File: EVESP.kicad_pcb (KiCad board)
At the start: 2 copper layers, 106 parts, among them J1 Screw_Terminal_01x08, J2 Screw_Terminal_01x06, J3 Conn_01x04, J4 Conn_01x16_Male, J5 Conn_01x16_Female, J6 Conn_01x20_Female, J7 Conn_01x20_Male, J8 Screw_Terminal_01x03, J9 Screw_Terminal_01x03, Q1 BC847, Q2 BC847, Q3 BC847, U1 LM7332, U2 MOC3063M, U3 MOC3063M, U4 MOC3063M, U5 LM7332

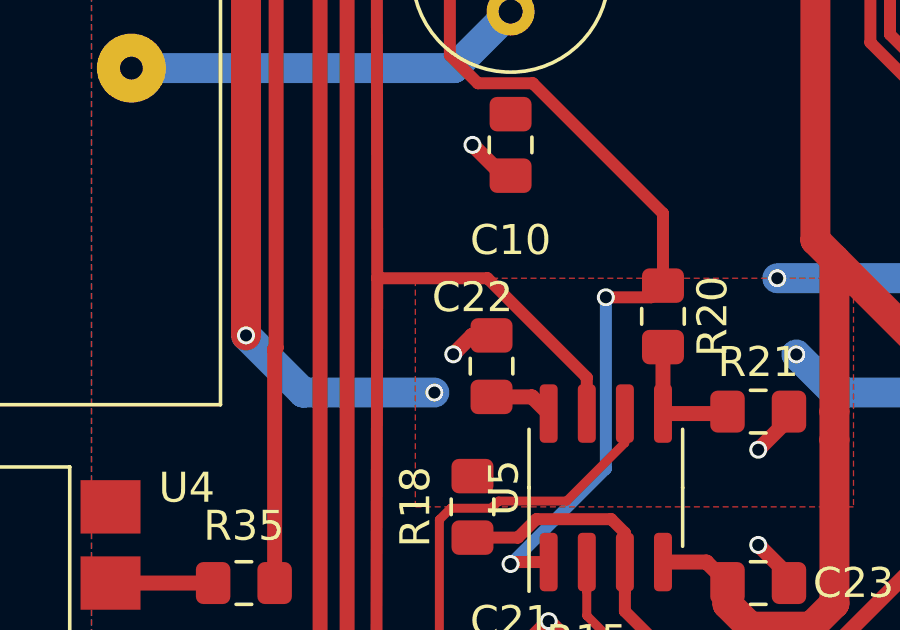
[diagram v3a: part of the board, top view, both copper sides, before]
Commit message: +12V connectivity fixed
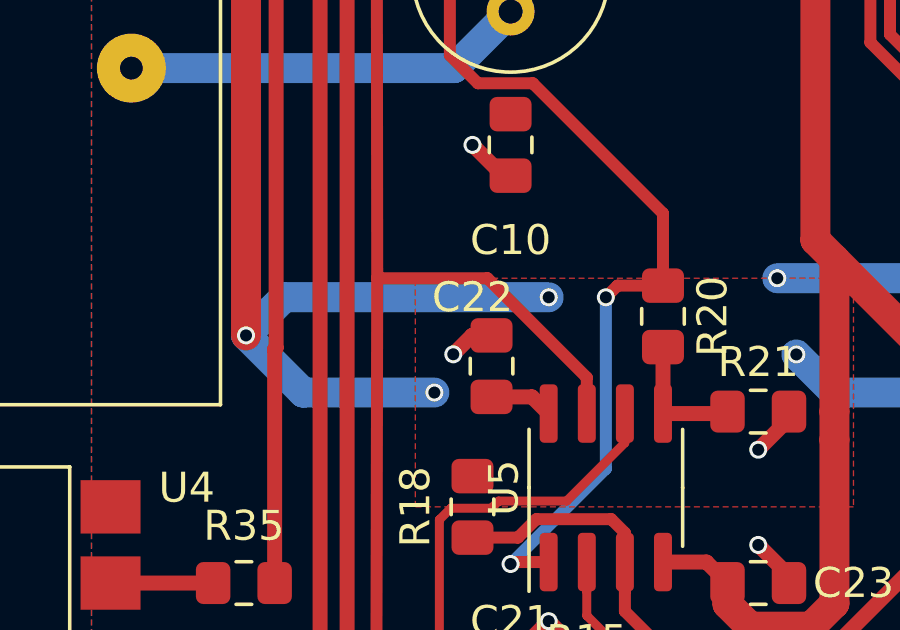
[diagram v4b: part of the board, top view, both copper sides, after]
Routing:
- net +12V: track 112.8 -> 123.4 mm, vias 4 -> 5
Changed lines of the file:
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@@
     (thickness 1.6)
     (drawings 0)
-    (tracks 612)
+    (tracks 615)
     (zones 0)
     (modules 106)
@@
   )
   (setup
-    (last_trace_width 0.5)
+    (last_trace_width 0.4)
     (user_trace_width 0.3)
     (user_trace_width 0.4)
@@
   (segment (start 94.615 133.35) (end 90.24099 133.35) (width 1) (layer B.Cu) (net 4))
   (segment (start 117.475 133.35) (end 118.11 133.35) (width 1) (layer B.Cu) (net 4))
+  (via (at 98.425 130.175) (size 0.6) (drill 0.4) (layers F.Cu B.Cu) (net 4))
+  (segment (start 89.60599 130.175) (end 98.425 130.175) (width 1) (layer B.Cu) (net 4))
+  (segment (start 88.33599 131.445) (end 89.60599 130.175) (width 1) (layer B.Cu) (net 4))
   (segment (start 131.69 142.175) (end 131.055 141.54) (width 0.5) (layer F.Cu) (net 5))
   (segment (start 131.69 142.875) (end 131.69 142.175) (width 0.5) (layer F.Cu) (net 5))
@@
   (segment (start 102.235 129.785) (end 102.235 127.379378) (width 0.4) (layer F.Cu) (net 68))
   (segment (start 98.425 139) (end 97.22 139) (width 0.4) (layer F.Cu) (net 68))
-  (via (at 97.155 139.065) (size 0.6) (drill 0.4) (layers F.Cu B.Cu) (net 68))
-  (segment (start 97.22 139) (end 97.155 139.065) (width 0.4) (layer F.Cu) (net 68))
-  (segment (start 100.33 130.175) (end 101.845 130.175) (width 0.4) (layer F.Cu) (net 68))
-  (segment (start 101.845 130.175) (end 102.235 129.785) (width 0.4) (layer F.Cu) (net 68))
-  (segment (start 100.33 135.89) (end 100.33 130.175) (width 0.4) (layer B.Cu) (net 68))
-  (via (at 100.33 130.175) (size 0.6) (drill 0.4) (layers F.Cu B.Cu) (net 68))
   (segment (start 97.155 139.065) (end 100.33 135.89) (width 0.4) (layer B.Cu) (net 68))
+  (via (at 100.33 130.175) (size 0.6) (drill 0.4) (layers F.Cu B.Cu) (net 68))
+  (segment (start 100.33 135.89) (end 100.33 130.175) (width 0.4) (layer B.Cu) (net 68))
+  (segment (start 97.22 139) (end 97.155 139.065) (width 0.4) (layer F.Cu) (net 68))
+  (via (at 97.155 139.065) (size 0.6) (drill 0.4) (layers F.Cu B.Cu) (net 68))
+  (segment (start 100.72 129.785) (end 100.33 130.175) (width 0.4) (layer F.Cu) (net 68))
+  (segment (start 102.235 129.785) (end 100.72 129.785) (width 0.4) (layer F.Cu) (net 68))
   (segment (start 100.965 139.975) (end 100.965 139) (width 0.4) (layer F.Cu) (net 69))
   (segment (start 102.235 141.91) (end 100.965 140.64) (width 0.4) (layer F.Cu) (net 69))
